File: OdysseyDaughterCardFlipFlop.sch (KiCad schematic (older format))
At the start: 1 part, among them X1 OdysseyDaughterCard

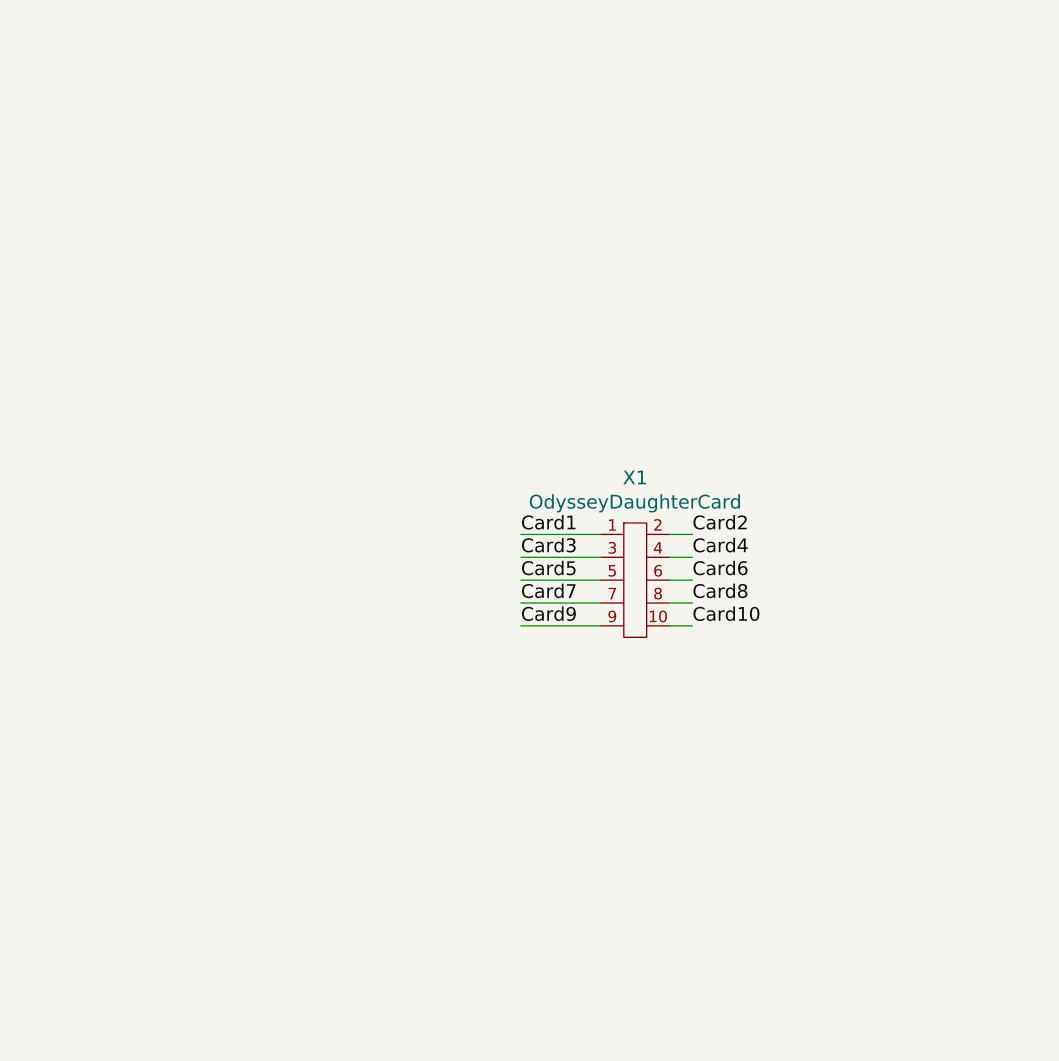
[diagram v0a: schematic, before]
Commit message: V0.1 of the flip flop daughter card
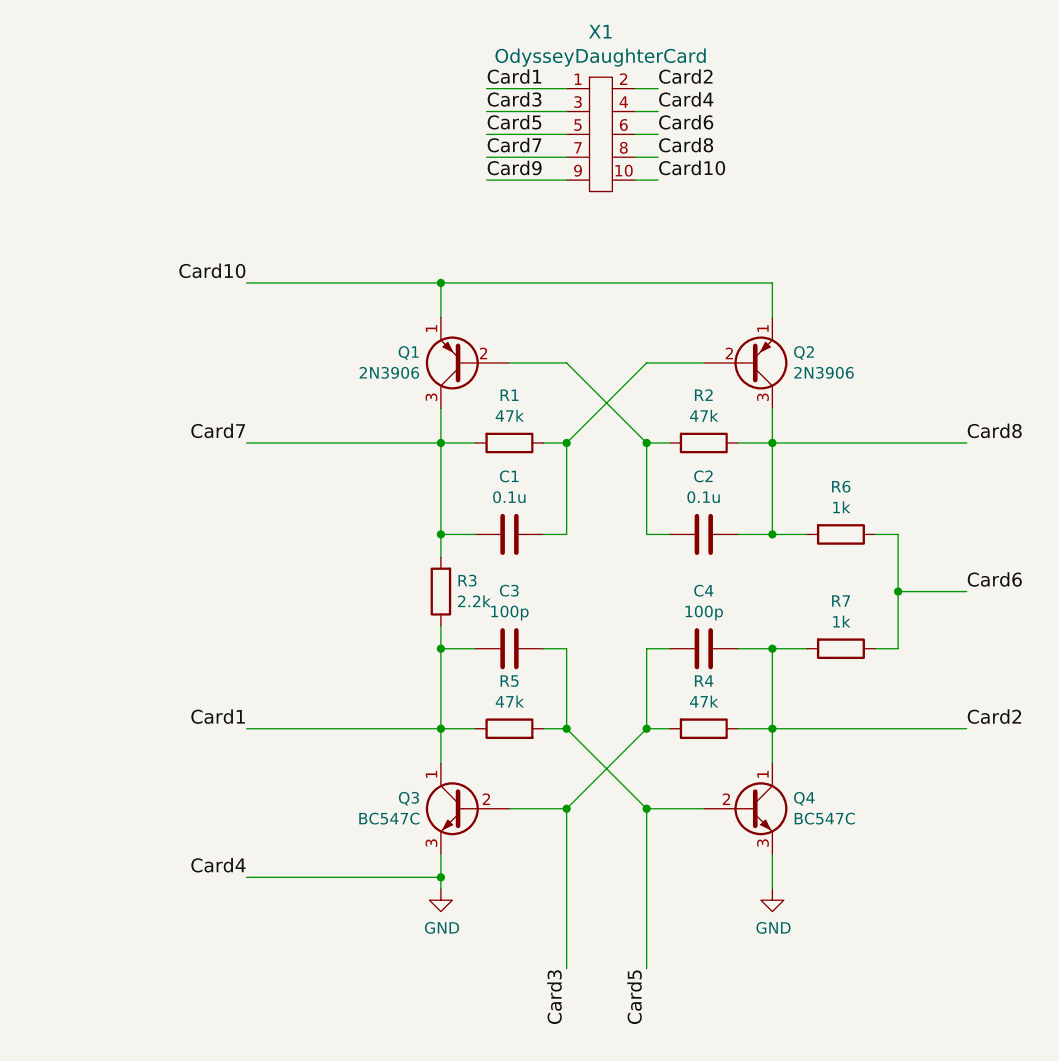
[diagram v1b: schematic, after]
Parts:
- added C1, C2: 0.1u, Capacitor_THT:C_Disc_D5.1mm_W3.2mm_P5.00mm, symbol Device:C
- added C3, C4: 100p, Capacitor_THT:C_Disc_D5.1mm_W3.2mm_P5.00mm, symbol Device:C
- added Q1, Q2: 2N3906, Package_TO_SOT_THT:TO-92_Inline, symbol Transistor_BJT:2N3906
- added Q3, Q4: BC547C, Package_TO_SOT_THT:TO-92_Inline, symbol Transistor_BJT:BC547
- added R1, R2, R4, R5: 47k, Resistor_THT:R_Axial_DIN0207_L6.3mm_D2.5mm_P7.62mm_Horizontal, symbol Device:R
- added R3: 2.2k, Resistor_THT:R_Axial_DIN0207_L6.3mm_D2.5mm_P7.62mm_Horizontal, symbol Device:R
- added R6, R7: 1k, Resistor_THT:R_Axial_DIN0207_L6.3mm_D2.5mm_P7.62mm_Horizontal, symbol Device:R
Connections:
- net Card1: now also C3.2, Q3.1 (C), R3.1, R5.1
- net Card10: now also Q1.1 (E), Q2.1 (E)
- net Card2: now also C4.1, Q4.1 (C), R4.1, R7.2
- net Card3: now also C4.2, Q3.2 (B), R4.2
- net Card5: now also C3.1, Q4.2 (B), R5.2
- net Card6: now also R6.1, R7.1
- net Card7: now also C1.2, Q1.3 (C), R1.2, R3.2
- net Card8: now also C2.1, Q2.3 (C), R2.1, R6.2
- net Card4 renamed GND
- net GND: now also Q3.3 (E), Q4.3 (E)
- new net: C2.2, Q1.2 (B), R2.2
- new net: C1.1, Q2.2 (B), R1.1
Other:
- moved on the sheet: X1

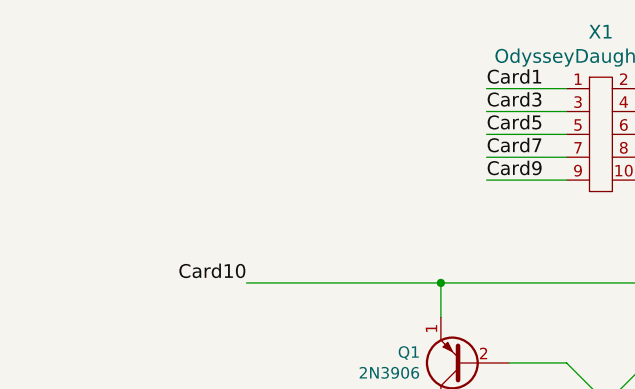
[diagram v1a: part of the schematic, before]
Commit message: R1.0 Flip-flop add header for extra player generator
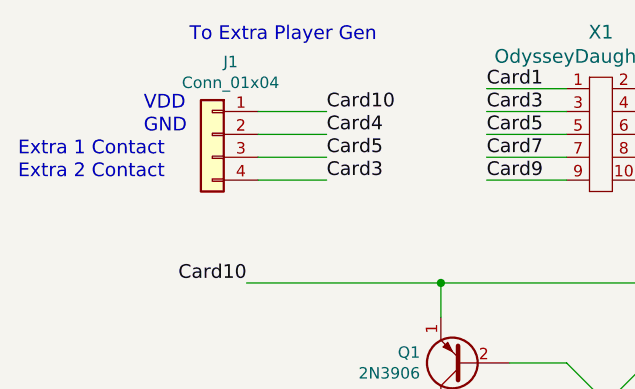
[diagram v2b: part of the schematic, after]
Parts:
- added J1: Conn_01x04, Connector_PinHeader_2.54mm:PinHeader_1x04_P2.54mm_Vertical, symbol Connector_Generic:Conn_01x04
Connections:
- net Card10: now also J1.1 (Pin_1)
- net Card3: now also J1.4 (Pin_4)
- net Card5: now also J1.3 (Pin_3)
- net GND: now also J1.2 (Pin_2)
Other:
- note added: "Extra 1 Contact"
- note added: "Extra 2 Contact"
- note added: "GND"
- note added: "To Extra Player Gen"
- note added: "VDD"
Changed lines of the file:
@@
 Sheet 1 1
 Title "Odyssey Daughter Card Flip Flop"
-Date "2018-08-18"
-Rev "0.1"
+Date "2018-11-23"
+Rev "1.0"
 Comp "University of Pittsburgh - Odyssey Restoration Project"
 Comment1 "Levi Burner"
@@
 Text Label 5750 5400 3    60   ~ 0
 Card5
+Wire Wire Line
+	4050 1850 4350 1850
+Wire Wire Line
+	4050 1950 4350 1950
+Text Label 4350 1850 0    60   ~ 0
+Card5
+Text Label 4350 1950 0    60   ~ 0
+Card3
+$Comp
+L Connector_Generic:Conn_01x04 J1
+U 1 1 5BF9F611
+P 3850 1750
+F 0 "J1" H 3770 2067 50  0000 C CNN
+F 1 "Conn_01x04" H 3770 1976 50  0000 C CNN
+F 2 "Connector_PinHeader_2.54mm:PinHeader_1x04_P2.54mm_Vertical" H 3850 1750 50  0001 C CNN
+F 3 "~" H 3850 1750 50  0001 C CNN
+	1    3850 1750
+	-1   0    0    -1
+$EndComp
+Wire Wire Line
+	4050 1650 4350 1650
+Wire Wire Line
+	4050 1750 4350 1750
+Text Label 4350 1650 0    60   ~ 0
+Card10
+Text Label 4350 1750 0    60   ~ 0
+Card4
+Text Notes 3750 1350 0    60   ~ 0
+To Extra Player Gen
+Text Notes 3550 1650 0    60   ~ 0
+VDD
+Text Notes 3550 1750 0    60   ~ 0
+GND
+Text Notes 3000 1850 0    60   ~ 0
+Extra 1 Contact
+Text Notes 3000 1950 0    60   ~ 0
+Extra 2 Contact
 $EndSCHEMATC

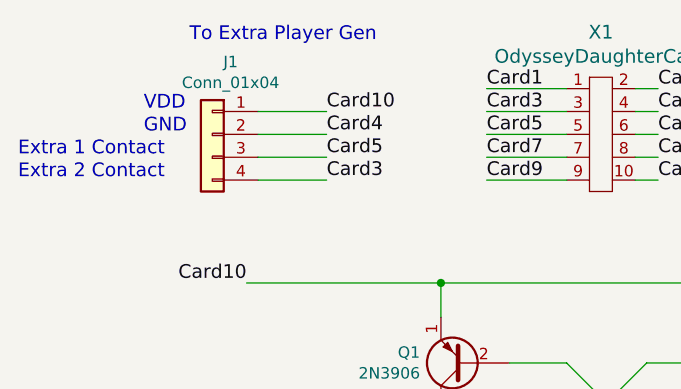
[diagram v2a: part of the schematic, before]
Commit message: Update to R1.1, remove power output for extra player generator
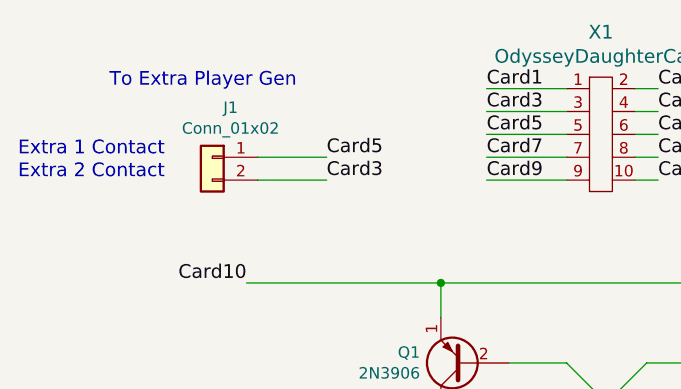
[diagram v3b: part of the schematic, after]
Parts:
- removed J1: Conn_01x04, Connector_PinHeader_2.54mm:PinHeader_1x04_P2.54mm_Vertical, symbol Connector_Generic:Conn_01x04
- added J1: Conn_01x02, Connector_PinHeader_2.54mm:PinHeader_1x02_P2.54mm_Vertical, symbol Connector_Generic:Conn_01x02
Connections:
- net Card3: now also J1.2 (Pin_2)
- net Card5: now also J1.1 (Pin_1)
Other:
- note removed: "GND"
- note removed: "VDD"
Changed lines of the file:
@@
 Sheet 1 1
 Title "Odyssey Daughter Card Flip Flop"
-Date "2018-11-23"
-Rev "1.0"
+Date "2019-02-16"
+Rev "1.1"
 Comp "University of Pittsburgh - Odyssey Restoration Project"
 Comment1 "Levi Burner"
@@
 Text Label 4350 1950 0    60   ~ 0
 Card3
-$Comp
-L Connector_Generic:Conn_01x04 J1
-U 1 1 5BF9F611
-P 3850 1750
-F 0 "J1" H 3770 2067 50  0000 C CNN
-F 1 "Conn_01x04" H 3770 1976 50  0000 C CNN
-F 2 "Connector_PinHeader_2.54mm:PinHeader_1x04_P2.54mm_Vertical" H 3850 1750 50  0001 C CNN
-F 3 "~" H 3850 1750 50  0001 C CNN
-	1    3850 1750
-	-1   0    0    -1
-$EndComp
-Wire Wire Line
-	4050 1650 4350 1650
-Wire Wire Line
-	4050 1750 4350 1750
-Text Label 4350 1650 0    60   ~ 0
-Card10
-Text Label 4350 1750 0    60   ~ 0
-Card4
-Text Notes 3750 1350 0    60   ~ 0
+Text Notes 3400 1550 0    60   ~ 0
 To Extra Player Gen
-Text Notes 3550 1650 0    60   ~ 0
-VDD
-Text Notes 3550 1750 0    60   ~ 0
-GND
 Text Notes 3000 1850 0    60   ~ 0
 Extra 1 Contact
 Text Notes 3000 1950 0    60   ~ 0
 Extra 2 Contact
+$Comp
+L Connector_Generic:Conn_01x02 J1
+U 1 1 5C6AAEE1
+P 3850 1850
+F 0 "J1" H 3770 2067 50  0000 C CNN
+F 1 "Conn_01x02" H 3770 1976 50  0000 C CNN
+F 2 "Connector_PinHeader_2.54mm:PinHeader_1x02_P2.54mm_Vertical" H 3850 1850 50  0001 C CNN
+F 3 "~" H 3850 1850 50  0001 C CNN
+	1    3850 1850
+	-1   0    0    -1
+$EndComp
 $EndSCHEMATC
